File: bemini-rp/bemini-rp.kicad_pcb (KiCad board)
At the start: 2 copper layers, 220 x 70 mm, 70 parts, among them J1 USB_C_Receptacle_USB2.0, K1 MX-NoLED, K10 MX-NoLED, K11 MX-NoLED, K12 MX-NoLED, K13 MX-NoLED, K2 MX-NoLED, K3 MX-NoLED, K4 MX-NoLED, K5 MX-NoLED, K6 MX-NoLED, K7 MX-NoLED, K8 MX-NoLED, K9 MX-NoLED, Q1 BSS138, SW1 BOOT, SW2 RESET, U1 RP2040, U2 W25Q128JV, U3 AP2112K-3.3, Y1 12MHz

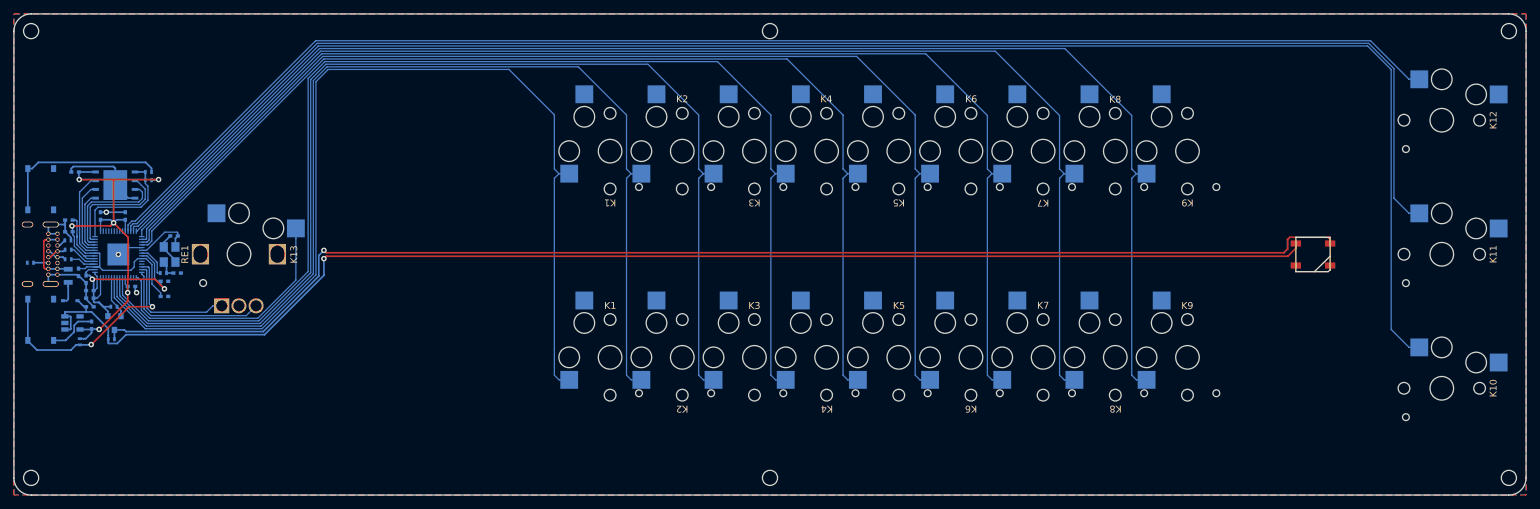
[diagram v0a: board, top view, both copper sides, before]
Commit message: update usb resistors
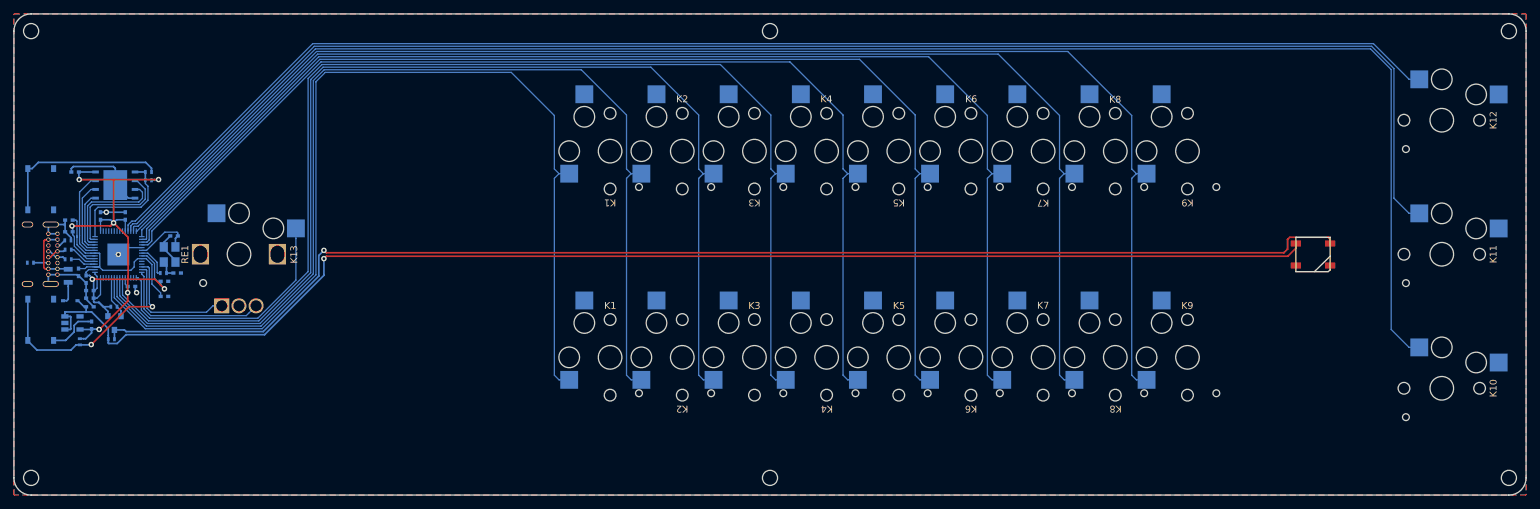
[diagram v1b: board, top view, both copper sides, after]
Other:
- board text added: "Bemini RP v2.0"
- board text removed: "Bemini RP v2.0 PROTO"
